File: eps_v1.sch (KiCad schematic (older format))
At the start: 21 parts, among them J7 PROGRAMMING PORT, J8 H_EPS, SW1 SW_RST, U1 ATMEGA32M1-MU, U8 SN65HVD230, U9 SST25VF016B, Y1 8MHz

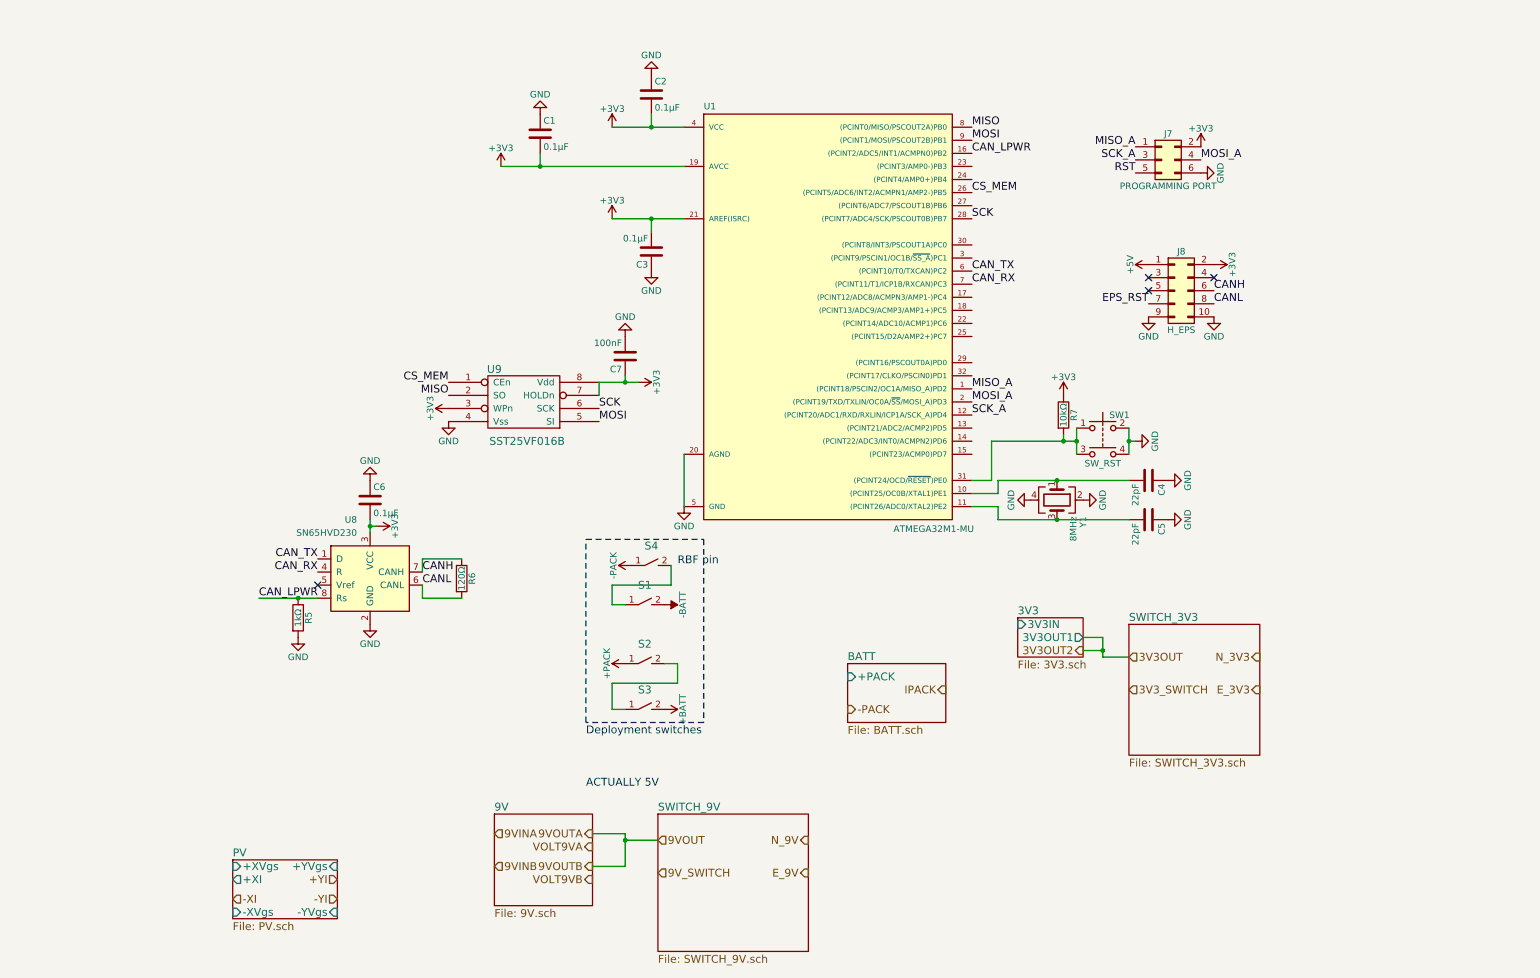
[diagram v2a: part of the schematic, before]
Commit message: PCB layout as of 2018-02-12
All that’s left to do is add deployment switches
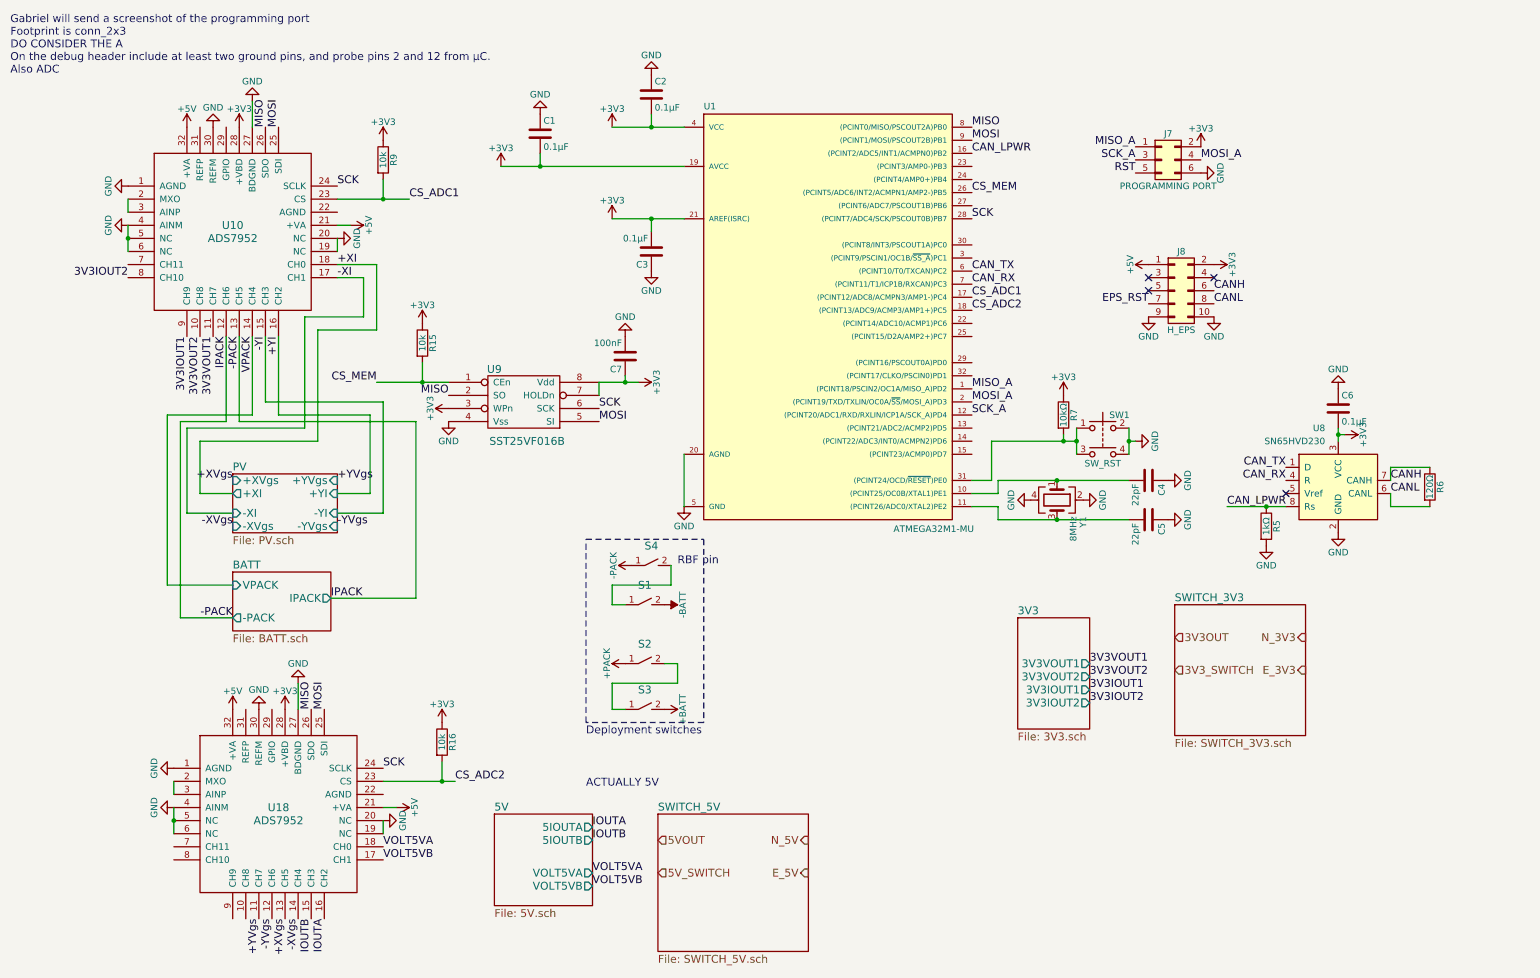
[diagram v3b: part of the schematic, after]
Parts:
- added R15, R16, R9: 10k, Resistors_SMD:R_0603_HandSoldering, symbol R
- added U10, U18: ADS7952, w_smd_qfn:pvqfn-n32, symbol ADS7952
- SW1: footprint (none) -> Buttons_Switches_SMD:SW_SPST_B3S-1000
- U8: footprint (none) -> Housings_SOIC:SOIC-8_3.9x4.9mm_Pitch1.27mm
- U9: footprint kicad-libraries:SOIC8 -> Housings_SOIC:SO-8_5.3x6.2mm_Pitch1.27mm
- Y1: footprint Housings_SOIC:SO-20_12.8x7.5mm_Pitch1.27mm -> Crystals:Crystal_SMD_Abracon_ABM3B-4pin_5.0x3.2mm
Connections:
- net +3V3: now also R15.1, R16.1, R9.1, U10.28 (+VBD), U18.28 (+VBD)
- net +5V: now also U10.21 (+VA), U10.32 (+VA), U18.21 (+VA), U18.32 (+VA)
- net +YI: now also U10.16 (CH2)
- net -PACK: now also U10.12 (CH6), U10.13 (CH5)
- net -XI: now also U10.17 (CH1)
- net -YI: now also U10.15 (CH3)
- net CS_MEM: now also R15.2
- net GND: now also U10.1 (AGND), U10.19 (NC), U10.20 (NC), U10.27 (BDGND), U10.30 (REFM), U10.4 (AINM), U10.5 (NC), U10.6 (NC), U18.1 (AGND), U18.19 (NC), U18.20 (NC), U18.27 (BDGND), U18.30 (REFM), U18.4 (AINM), U18.5 (NC), U18.6 (NC)
- net MISO: now also U10.26 (SDO), U18.26 (SDO)
- net MOSI: now also U10.25 (SDI), U18.25 (SDI)
- net SCK: now also U10.24 (SCLK), U18.24 (SCLK)
- net CS_ADC1: now reaches U1.17 ((PCINT12/ADC8/ACMPN3/AMP1-)PC4)
- net CS_ADC1: now also R9.2, U10.23 (CS)
- net CS_ADC2: now reaches U1.18 ((PCINT13/ADC9/ACMP3/AMP1+)PC5)
- net CS_ADC2: now also R16.2, U18.23 (CS)
- new net: U10.2 (MXO), U10.3 (AINP)
- new net: U18.2 (MXO), U18.3 (AINP)
- new net +XI: U10.18 (CH0)
- new net +XVgs: U18.13 (CH5)
- new net +YVgs: U18.11 (CH7)
- new net -XVgs: U18.14 (CH4)
- new net -YVgs: U18.12 (CH6)
- new net 3V3IOUT1: U10.9 (CH9)
- new net 3V3IOUT2: U10.8 (CH10)
- new net 3V3VOUT1: U10.11 (CH7)
- new net 3V3VOUT2: U10.10 (CH8)
- new net IOUTA: U18.16 (CH2)
- new net IOUTB: U18.15 (CH3)
- new net VOLT5VA: U18.18 (CH0)
- new net VOLT5VB: U18.17 (CH1)
- new net VPACK: U10.14 (CH4)
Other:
- note added: "Gabriel will send a screenshot of the programming port\nFootprint is conn_2x3\nDO CONSIDER THE A\nOn the debug header include at least two ground pins, and probe pins 2 and 12 from µC.\nAlso ADC"
- moved on the sheet: C6, R5, R6, U8

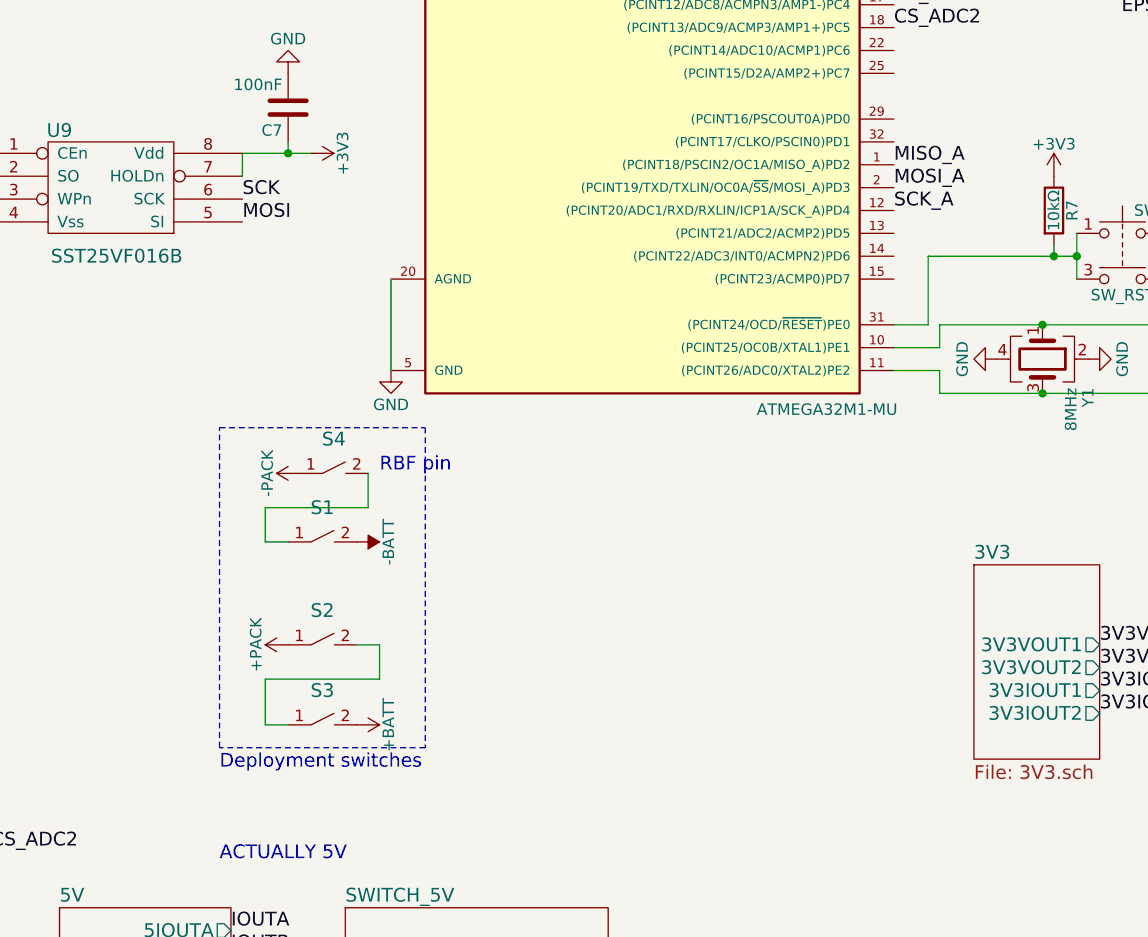
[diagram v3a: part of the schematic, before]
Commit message: Added deployment/RBL switches and debug headers to EPS board
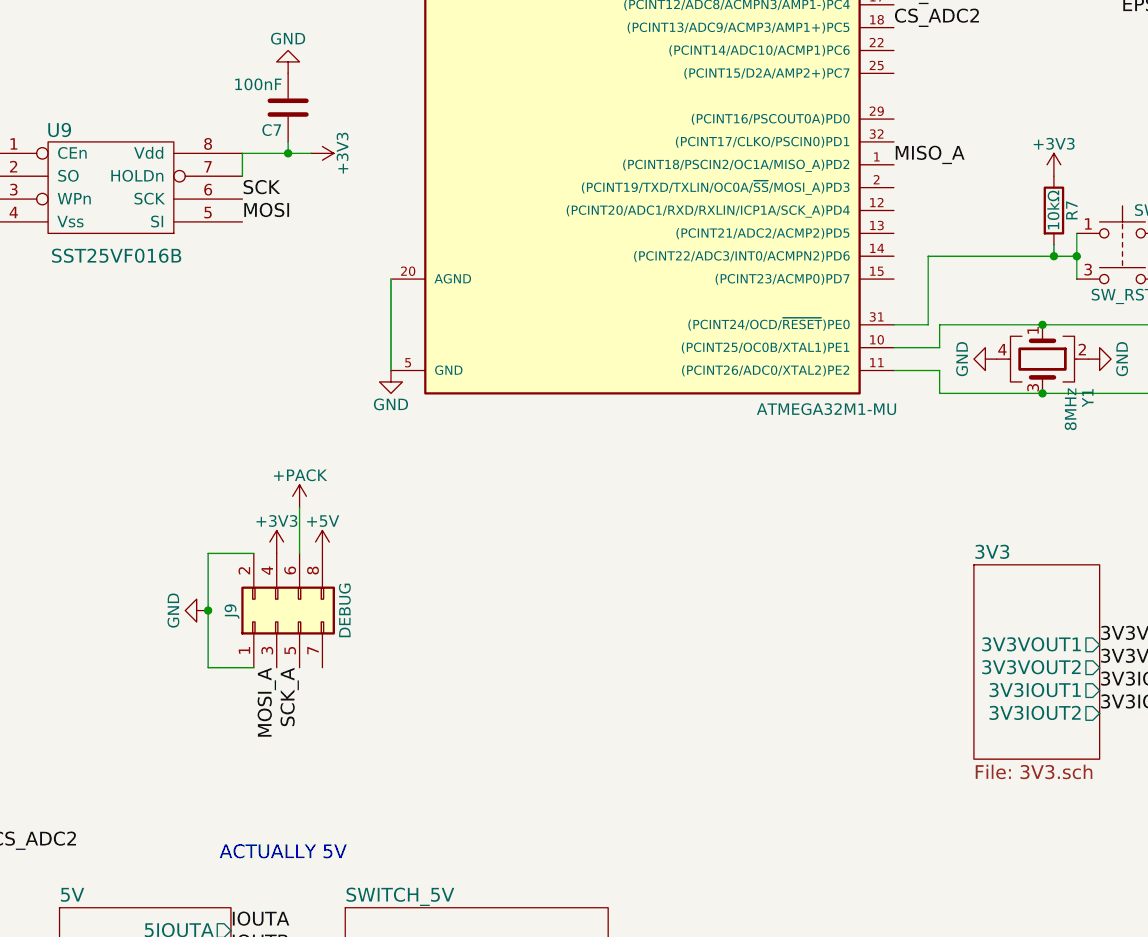
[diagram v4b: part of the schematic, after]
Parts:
- removed S1, S2, S3, S4: switch, symbol switch
- added J9: DEBUG, Pin_Headers:Pin_Header_Straight_2x04_Pitch2.54mm, symbol Conn_02x04_Odd_Even
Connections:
- net +3V3: now also J9.4 (Pin_4)
- net +5V: now also J9.8 (Pin_8)
- net +PACK: now also J9.6 (Pin_6)
- net GND: now also J9.1 (Pin_1), J9.2 (Pin_2)
- net MOSI_A: now also J9.3 (Pin_3); no longer U1.2 ((PCINT19/TXD/TXLIN/OC0A/~SS~/MOSI_A)PD3)
- net SCK_A: now also J9.5 (Pin_5); no longer U1.12 ((PCINT20/ADC1/RXD/RXLIN/ICP1A/SCK_A)PD4)
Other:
- note removed: "Deployment switches\n"
- note removed: "RBF pin"

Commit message: Exported EPS board
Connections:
- net EPS_RST: now also R7.2, SW1.1, SW1.3, U1.31 ((PCINT24/OCD/~RESET~)PE0)
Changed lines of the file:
@@
 	0    -1   -1   0
 $EndComp
+Text Label 7900 3700 2    60   ~ 0
+EPS_RST
 $EndSCHEMATC
